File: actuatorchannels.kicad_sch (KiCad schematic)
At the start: 102 parts, among them J10 ACT CH9, J11 ACT CH10, J12 ACT CH11, J13 ACT CH12, J14 ACT CH13, J15 ACT CH14, J16 ACT CH15, J17 ACT CH16, J2 ACT CH1, J3 ACT CH2, J4 ACT CH3, J5 ACT CH4, J6 ACT CH5, J7 ACT CH6, J8 ACT CH7, J9 ACT CH8, U10 TLP241A, U11 TLP241A, U12 TLP241A, U13 TLP241A, U14 TLP241A, U15 TLP241A, U16 TLP241A, U17 TLP241A, U18 TLP241A, U19 PCA9534, U20 PCA9534, U3 TLP241A, U4 TLP241A, U5 TLP241A, U6 TLP241A, U7 TLP241A, U8 TLP241A, U9 TLP241A

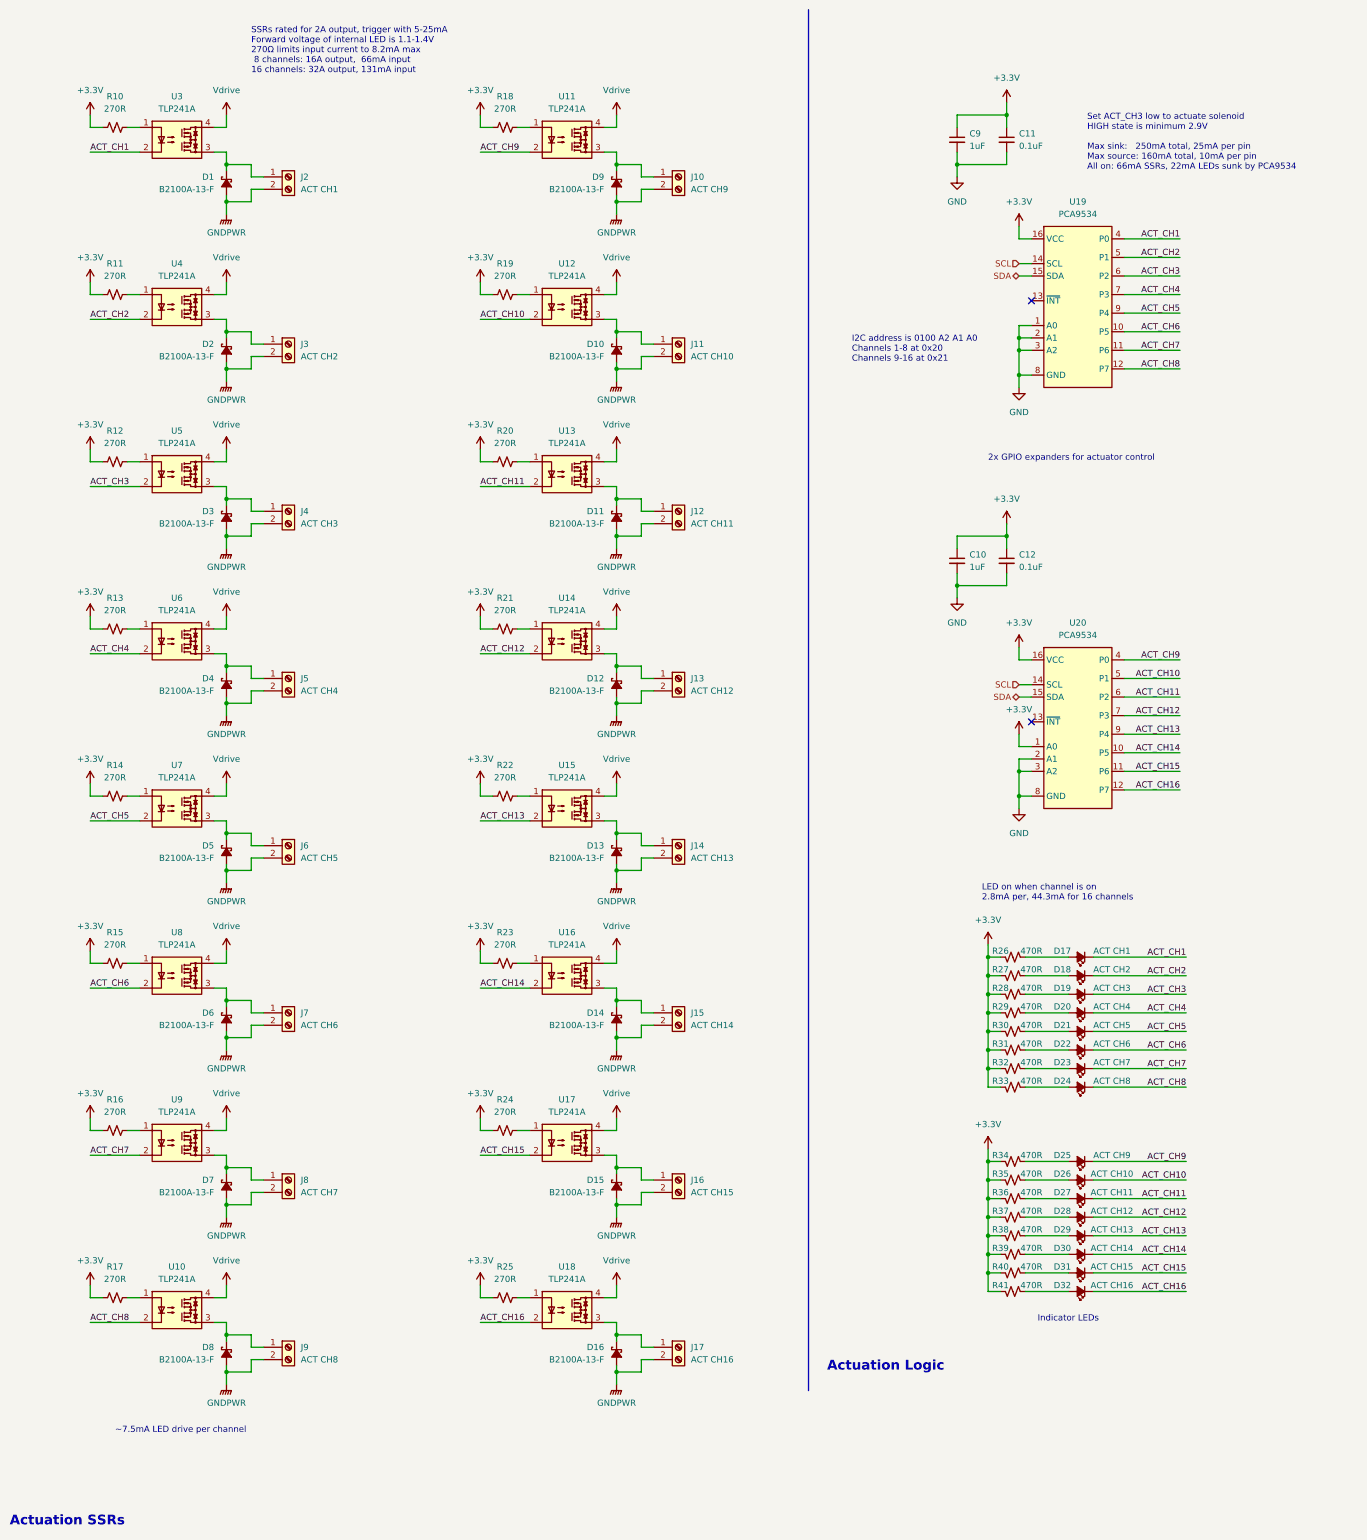
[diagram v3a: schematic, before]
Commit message: Added feedback indicator LED buffer and made changes to notes
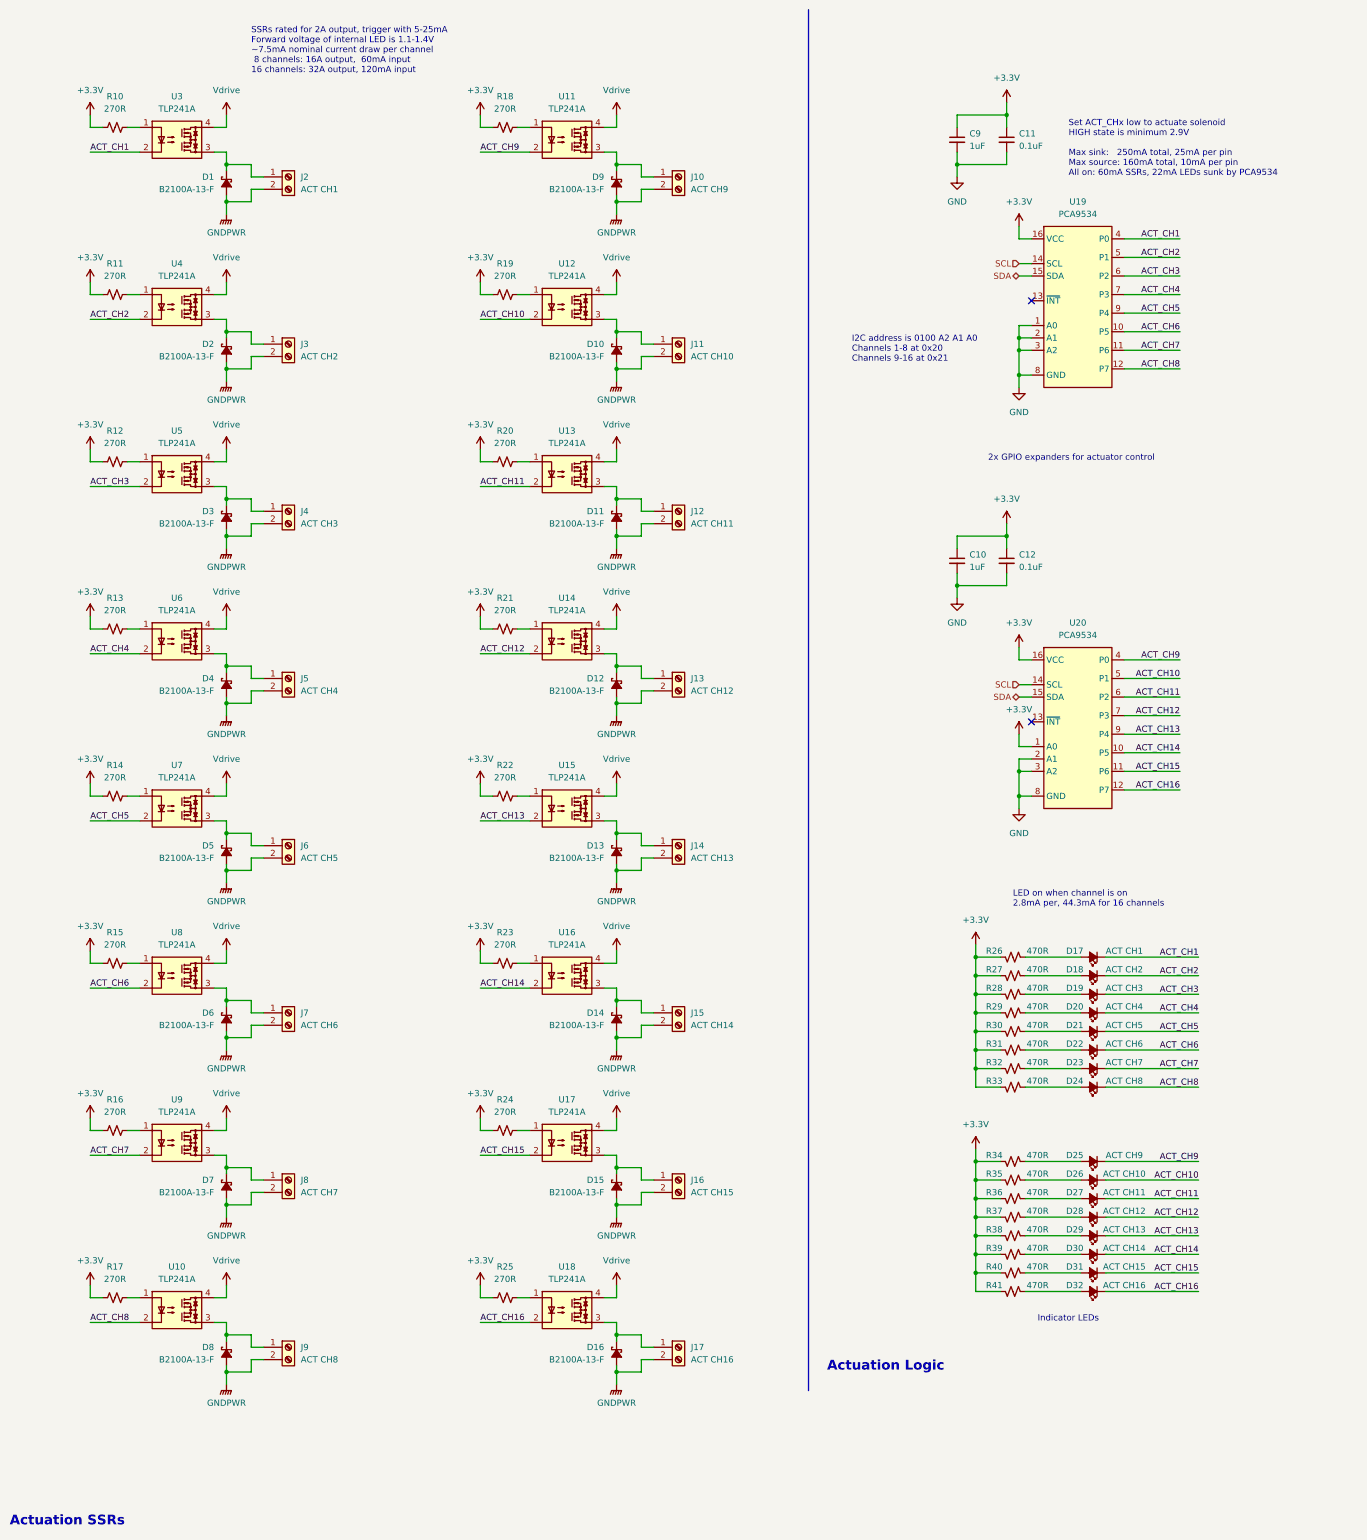
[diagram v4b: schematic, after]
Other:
- note added: "SSRs rated for 2A output, trigger with 5-25mA Forward voltage of internal LED is 1.1-1.4V ~7.5mA nominal current draw per channel 8 channels: 16A output, 60mA input 16 channels: 32A output, 120mA input"
- note added: "Set ACT_CHx low to actuate solenoid HIGH state is minimum 2.9V Max sink: 250mA total, 25mA per pin Max source: 160mA total, 10mA per pin All on: 60mA SSRs, 22mA LEDs sunk by PCA9534"
- note removed: "SSRs rated for 2A output, trigger with 5-25mA Forward voltage of internal LED is 1.1-1.4V 270Ω limits input current to 8.2mA max 8 channels: 16A output, 66mA input 16 channels: 32A output, 131mA input"
- note removed: "Set ACT_CH3 low to actuate solenoid HIGH state is minimum 2.9V Max sink: 250mA total, 25mA per pin Max source: 160mA total, 10mA per pin All on: 66mA SSRs, 22mA LEDs sunk by PCA9534"
- note removed: "~7.5mA LED drive per channel"
- moved on the sheet: D17, D18, D19, D20, D21, D22, D23, D24, D25, D26, D27, D28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

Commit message: Footprints, some part selection, external power outputs
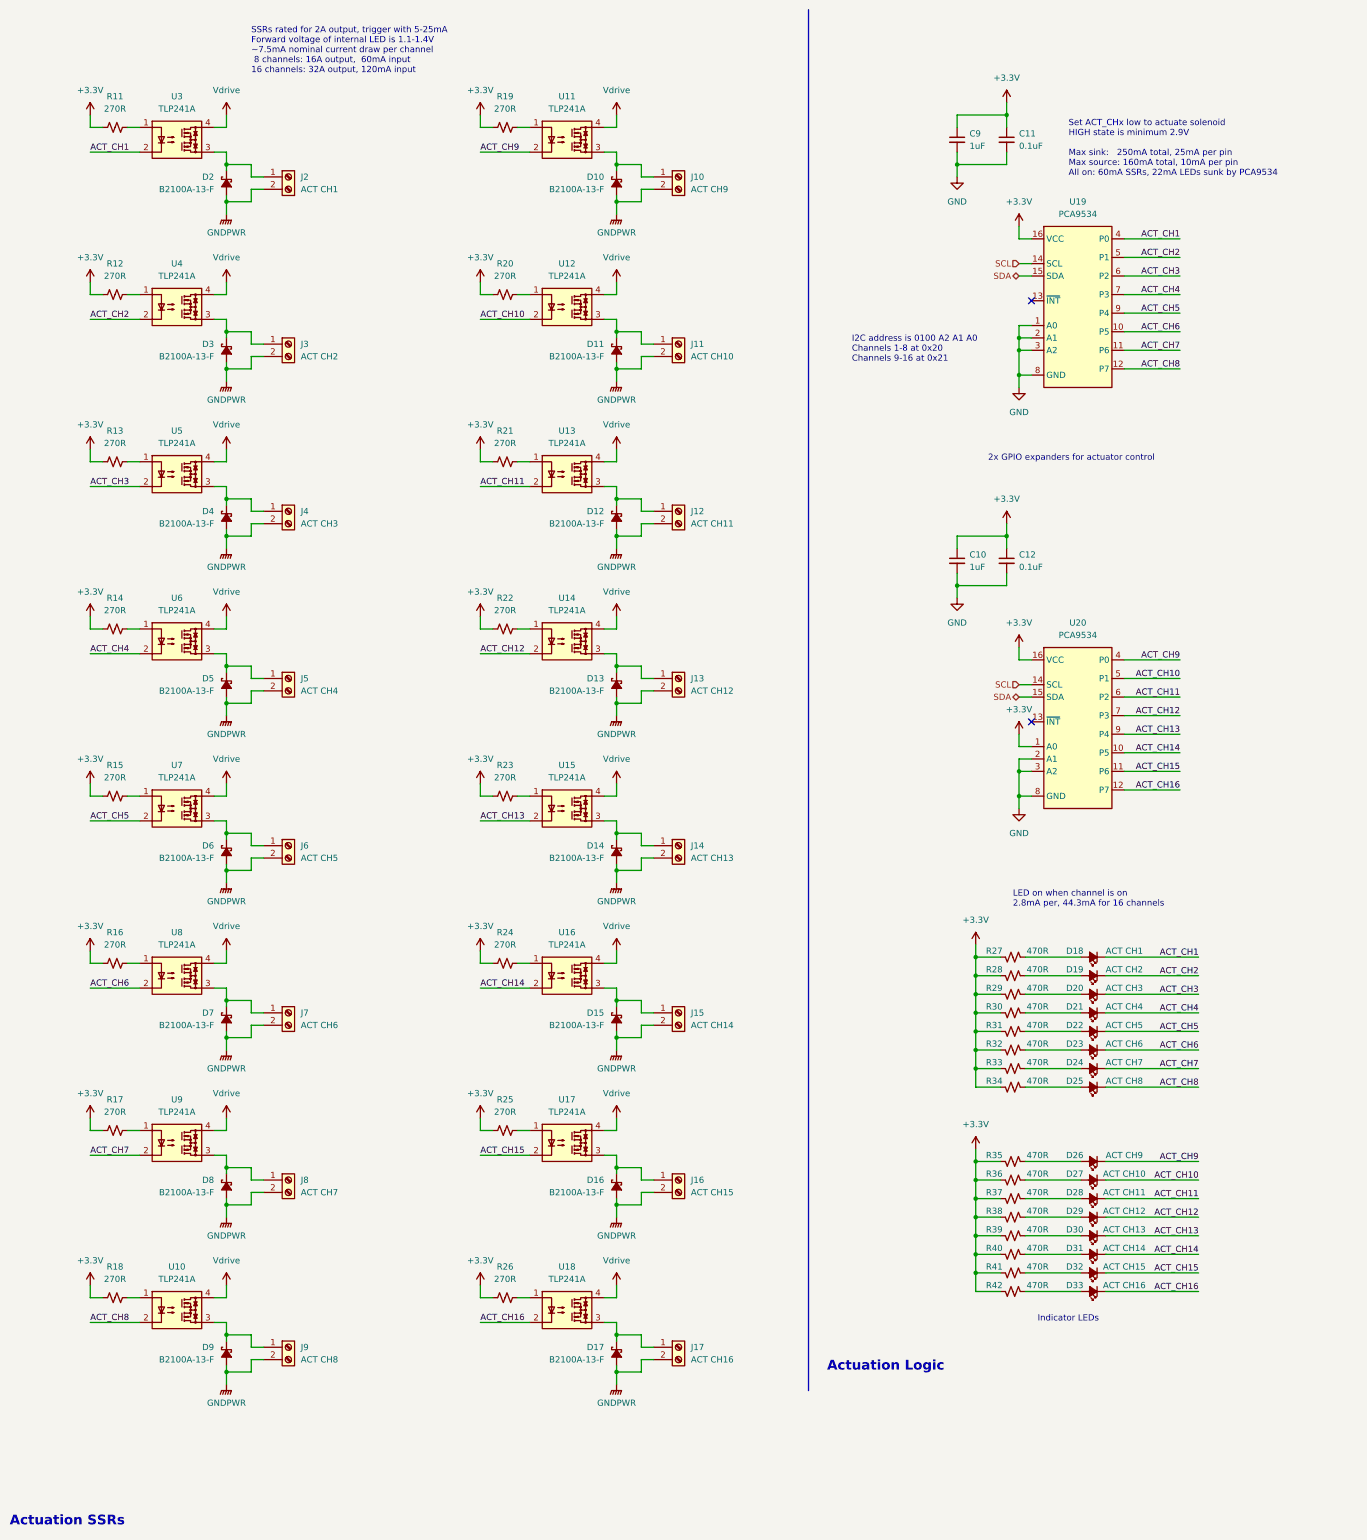
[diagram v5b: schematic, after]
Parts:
- D18: renamed from D17; footprint (none) -> LED_SMD:LED_0603_1608Metric
- D19: renamed from D18; footprint (none) -> LED_SMD:LED_0603_1608Metric
- D20: renamed from D19; footprint (none) -> LED_SMD:LED_0603_1608Metric
- D21: renamed from D20; footprint (none) -> LED_SMD:LED_0603_1608Metric
- D22: renamed from D21; footprint (none) -> LED_SMD:LED_0603_1608Metric
- D23: renamed from D22; footprint (none) -> LED_SMD:LED_0603_1608Metric
- D24: renamed from D23; footprint (none) -> LED_SMD:LED_0603_1608Metric
- D25: renamed from D24; footprint (none) -> LED_SMD:LED_0603_1608Metric
- D26: renamed from D25; footprint (none) -> LED_SMD:LED_0603_1608Metric
- D27: renamed from D26; footprint (none) -> LED_SMD:LED_0603_1608Metric
- D28: renamed from D27; footprint (none) -> LED_SMD:LED_0603_1608Metric
- D29: renamed from D28; footprint (none) -> LED_SMD:LED_0603_1608Metric
- D30: renamed from D29; footprint (none) -> LED_SMD:LED_0603_1608Metric
- D31: renamed from D30; footprint (none) -> LED_SMD:LED_0603_1608Metric
- D32: renamed from D31; footprint (none) -> LED_SMD:LED_0603_1608Metric
- D33: renamed from D32; footprint (none) -> LED_SMD:LED_0603_1608Metric
- R27: renamed from R26; footprint (none) -> Resistor_SMD:R_0603_1608Metric
- R28: renamed from R27; footprint (none) -> Resistor_SMD:R_0603_1608Metric
- R29: renamed from R28; footprint (none) -> Resistor_SMD:R_0603_1608Metric
- R30: renamed from R29; footprint (none) -> Resistor_SMD:R_0603_1608Metric
- R31: renamed from R30; footprint (none) -> Resistor_SMD:R_0603_1608Metric
- R32: renamed from R31; footprint (none) -> Resistor_SMD:R_0603_1608Metric
- R33: renamed from R32; footprint (none) -> Resistor_SMD:R_0603_1608Metric
- R34: renamed from R33; footprint (none) -> Resistor_SMD:R_0603_1608Metric
- R35: renamed from R34; footprint (none) -> Resistor_SMD:R_0603_1608Metric
- R36: renamed from R35; footprint (none) -> Resistor_SMD:R_0603_1608Metric
- R37: renamed from R36; footprint (none) -> Resistor_SMD:R_0603_1608Metric
- R38: renamed from R37; footprint (none) -> Resistor_SMD:R_0603_1608Metric
- R39: renamed from R38; footprint (none) -> Resistor_SMD:R_0603_1608Metric
- R40: renamed from R39; footprint (none) -> Resistor_SMD:R_0603_1608Metric
- R41: renamed from R40; footprint (none) -> Resistor_SMD:R_0603_1608Metric
- R42: renamed from R41; footprint (none) -> Resistor_SMD:R_0603_1608Metric
- U10, U11, U12, U13, U14, U15, U16, U17, U18, U3, U4, U5, U6, U7, U8, U9: footprint actuation:11-5B2S -> actuation:TLP241A
- renumbered D9 to D10, D10 to D11, D11 to D12, D12 to D13, D13 to D14, D14 to D15, D15 to D16, D16 to D17, D1 to D2, D2 to D3, D3 to D4, D4 to D5, D5 to D6, D6 to D7, D7 to D8, D8 to D9, R10 to R11, R11 to R12, R12 to R13, R13 to R14, R14 to R15, R15 to R16, R16 to R17, R17 to R18, R18 to R19, R19 to R20, R20 to R21, R21 to R22, R22 to R23, R23 to R24, R24 to R25, R25 to R26

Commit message: LED MPNs and new status indicator
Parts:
- D18, D19, D20, D21, D22, D23, D24, D25, D26, D27, D28, D29, D30, D31, D32, D33: MPN (none) -> LTST-C191KRKT
